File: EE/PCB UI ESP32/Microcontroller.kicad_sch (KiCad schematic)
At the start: 43 parts, among them J1 T1M-05-F-SV-L, J3 KH-TYPE-C-16P, Q1 SS8050, Q2 SS8050, SW1 EN, U1 CH340C, U2 ESP32-WROOM-32E, U5 PEC16-4215F-S0024

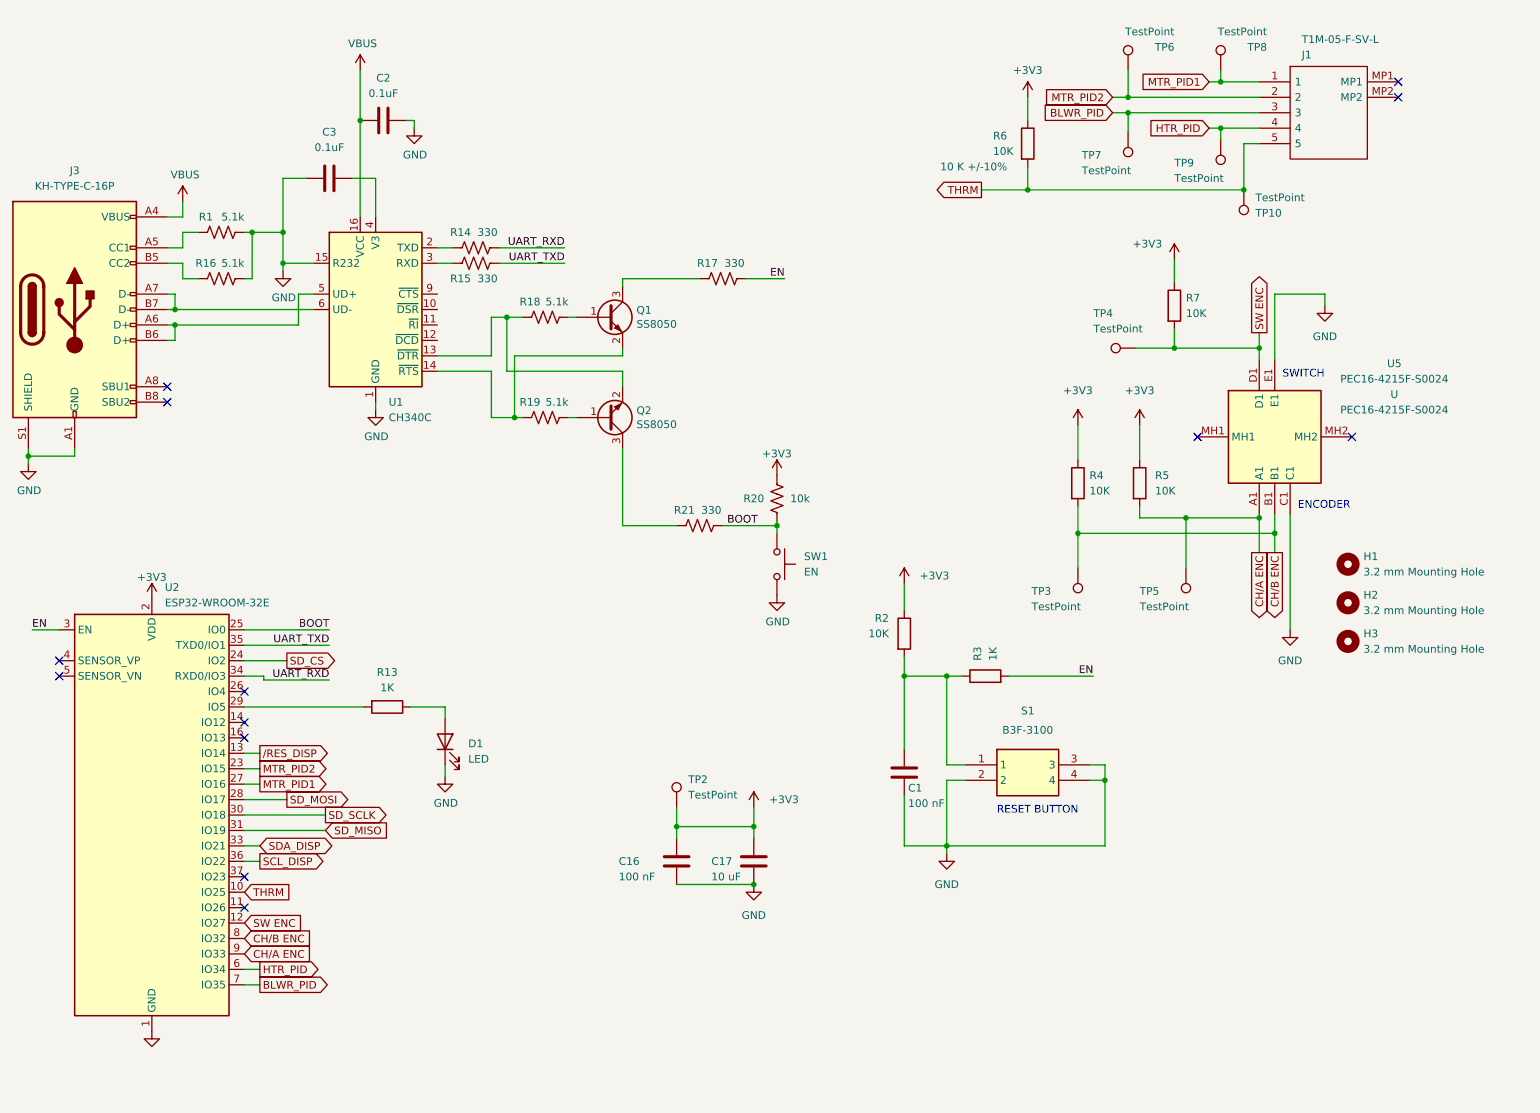
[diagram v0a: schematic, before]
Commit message: Finished first draft of ESP32-UI board
And moved around footprints, 3D models, etc. to match.
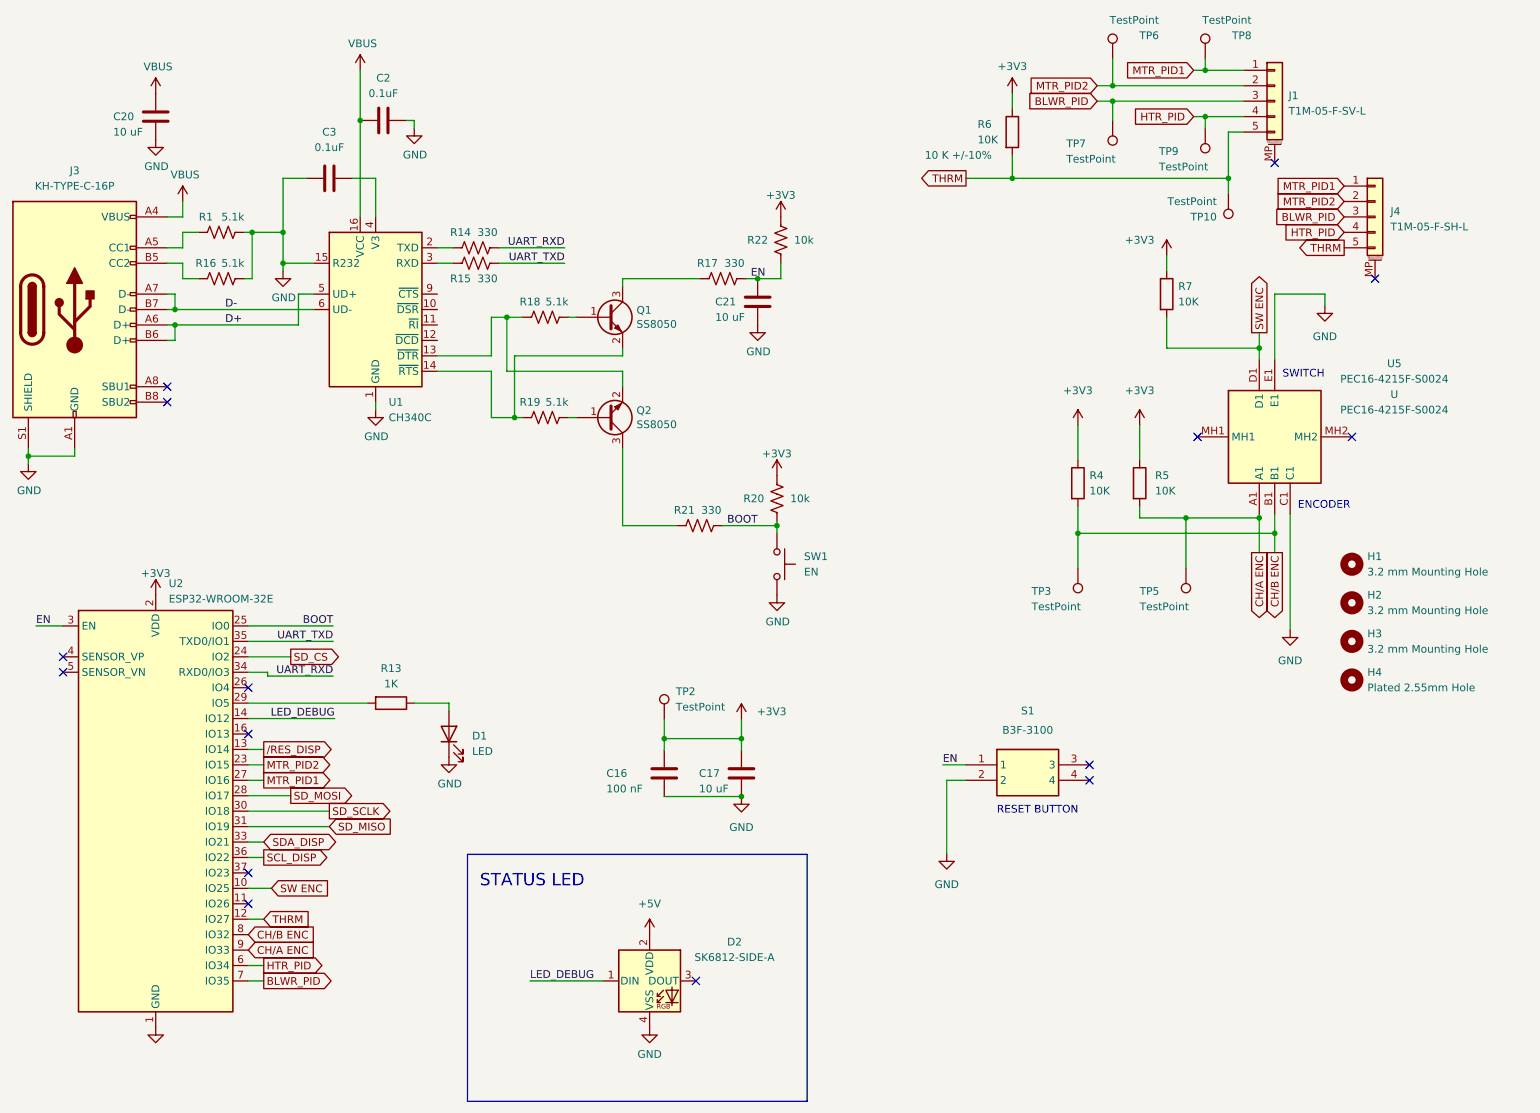
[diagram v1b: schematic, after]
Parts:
- removed C1: 100 nF, Capacitor_SMD:C_0603_1608Metric, symbol Device:C
- removed J1: T1M-05-F-SV-L, T1M-05-F-SV-L:T1M05FSVL, symbol T1M-05-F-SV-L:T1M-05-F-SV-L
- removed R2: 10K, Resistor_SMD:R_0805_2012Metric, symbol Device:R
- removed R3: 1K, Resistor_SMD:R_0805_2012Metric, symbol Device:R
- removed TP4: TestPoint, TestPoint:TestPoint_Pad_D1.5mm, symbol Connector:TestPoint
- added C20, C21: 10 uF, Capacitor_SMD:C_0805_2012Metric, symbol Device:C
- added D2: SK6812-SIDE-A, DaisyBio_Mira:SK6812-SIDE-A, symbol DaisyBio_Mira:SK6812-SIDE-A
- added H4: Plated 2.55mm Hole, MountingHole:MountingHole_3.2mm_M3, symbol Mechanical:MountingHole
- added J1: T1M-05-F-SV-L, DaisyBio_Mira:T1M-05-X-SV-L-Y, symbol Connector_Generic_MountingPin:Conn_01x05_MountingPin
- added J4: T1M-05-F-SH-L, DaisyBio_Mira:T1M-05-X-SH-L, symbol Connector_Generic_MountingPin:Conn_01x05_MountingPin
- added R22: 10k, Resistor_SMD:R_0603_1608Metric, symbol Device:R_US
- S1: footprint B3F-3100:B3F3100 -> DaisyBio_Mira:B3F3100
- U5: footprint PEC16-4215F-S0024:PEC164120FS0012 -> DaisyBio_Mira:PEC164120FS0012
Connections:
- net +3V3: now also R22.2
- net BLWR_PID: now also J1.3 (Pin_3), J4.3 (Pin_3)
- net EN: now also S1.1, C21.1, R22.1
- net GND: now also C20.2, C21.2, D2.4 (VSS); no longer S1.3, S1.4
- net HTR_PID: now also J1.4 (Pin_4), J4.4 (Pin_4)
- net MTR_PID1: now also J1.1 (Pin_1), J4.1 (Pin_1)
- net MTR_PID2: now also J1.2 (Pin_2), J4.2 (Pin_2)
- net SW ENC: now also U2.10 (IO25); no longer U2.12 (IO27)
- net THRM: now also U2.12 (IO27), J1.5 (Pin_5), J4.5 (Pin_5); no longer U2.10 (IO25)
- net VBUS: now also C20.1
- net LED_DEBUG: now reaches U2.14 (IO12)
- net LED_DEBUG: now also D2.1 (DIN)
- net D+: now reaches J3.A6 (D+), J3.B6 (D+), U1.5 (UD+)
- net D-: now reaches J3.A7 (D-), J3.B7 (D-), U1.6 (UD-)
- new net +5V: D2.2 (VDD)
- no-connect marks 13 -> 15
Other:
- note added: "STATUS LED"
- moved on the sheet: C16, C17, D1, H1, H2, H3, R13, R6, R7, TP10, TP2, TP6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
